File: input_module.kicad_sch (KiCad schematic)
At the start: 13 parts, among them Q14 BC846

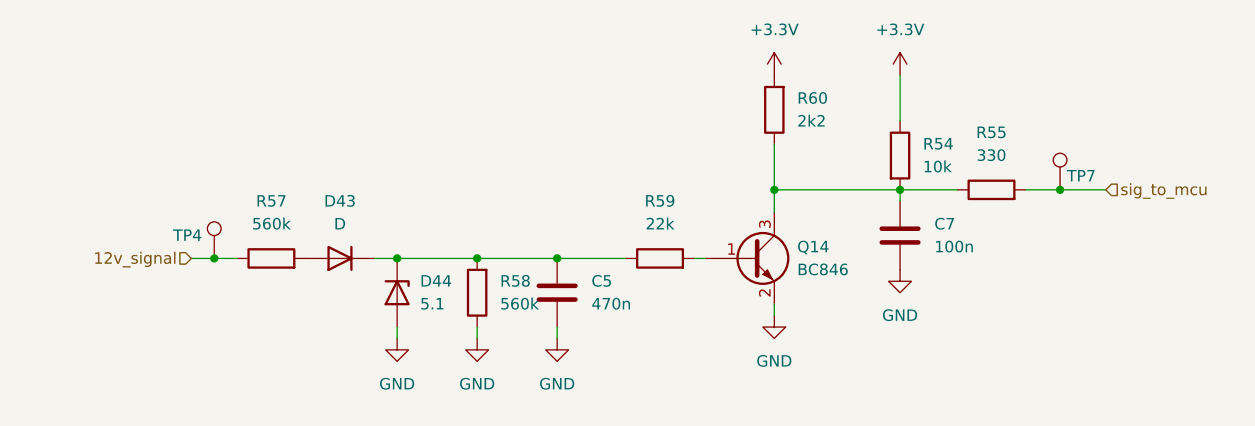
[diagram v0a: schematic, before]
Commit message: Schematic sites change
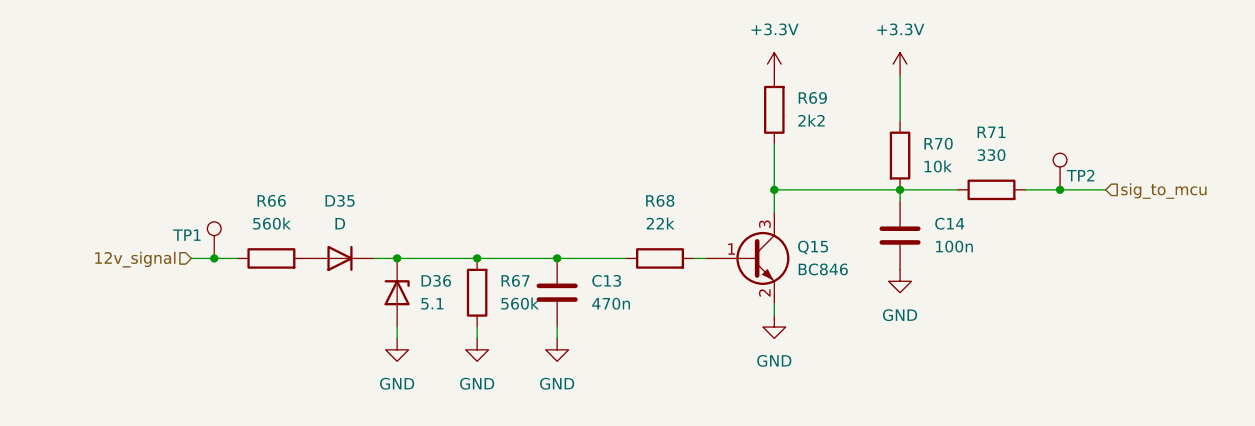
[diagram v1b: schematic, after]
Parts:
- renumbered C5 to C13, C7 to C14, D43 to D35, D44 to D36, Q14 to Q15, R57 to R66, R58 to R67, R59 to R68, R60 to R69, R54 to R70, R55 to R71, TP4 to TP1, TP7 to TP2

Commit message: mos leds drivers
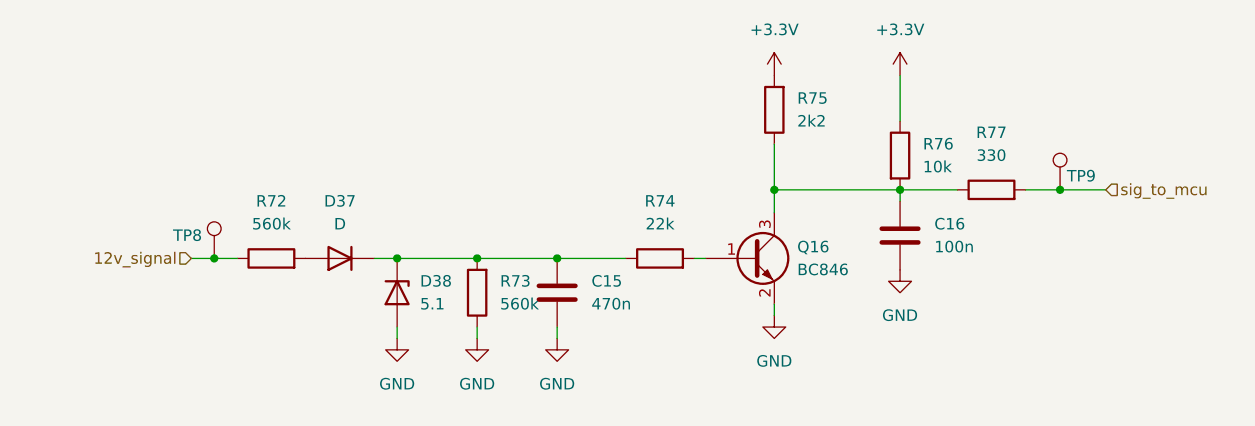
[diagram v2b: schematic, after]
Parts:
- renumbered C13 to C15, C14 to C16, D35 to D37, D36 to D38, Q15 to Q16, R66 to R72, R67 to R73, R68 to R74, R69 to R75, R70 to R76, R71 to R77, TP1 to TP8, TP2 to TP9
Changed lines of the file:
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@@
 		(dnp no)
 		(fields_autoplaced yes)
-		(property "Reference" "C13"
+		(property "Reference" "C15"
 			(at 118.11 62.2299 0)
 			(effects
@@
 		(on_board yes)
 		(dnp no)
-		(property "Reference" "TP1"
+		(property "Reference" "TP8"
 			(at 71.628 57.15 0)
 			(effects
@@
 		(dnp no)
 		(fields_autoplaced yes)
-		(property "Reference" "R67"
+		(property "Reference" "R73"
 			(at 107.95 62.2299 0)
 			(effects
@@
 		(dnp no)
 		(fields_autoplaced yes)
-		(property "Reference" "R68"
+		(property "Reference" "R74"
 			(at 125.73 53.34 90)
 			(effects
@@
 		(dnp no)
 		(fields_autoplaced yes)
-		(property "Reference" "#PWR061"
+		(property "Reference" "#PWR068"
 			(at 152.4 67.31 0)
 			(effects
@@
 		(on_board yes)
 		(dnp no)
-		(property "Reference" "TP2"
+		(property "Reference" "TP9"
 			(at 170.942 50.546 0)
 			(effects
@@
 		(dnp no)
 		(fields_autoplaced yes)
-		(property "Reference" "#PWR056"
+		(property "Reference" "#PWR063"
 			(at 105.41 74.93 0)
 			(effects
@@
 		(dnp no)
 		(fields_autoplaced yes)
-		(property "Reference" "R70"
+		(property "Reference" "R76"
 			(at 154.94 46.9899 0)
 			(effects
@@
 		(dnp no)
 		(fields_autoplaced yes)
-		(property "Reference" "R69"
+		(property "Reference" "R75"
 			(at 140.97 41.9099 0)
 			(effects
@@
 		(dnp no)
 		(fields_autoplaced yes)
-		(property "Reference" "D35"
+		(property "Reference" "D37"
 			(at 90.17 53.34 0)
 			(effects
@@
 		(dnp no)
 		(fields_autoplaced yes)
-		(property "Reference" "#PWR055"
+		(property "Reference" "#PWR062"
 			(at 96.52 74.93 0)
 			(effects
@@
 		(dnp no)
 		(fields_autoplaced yes)
-		(property "Reference" "R71"
+		(property "Reference" "R77"
 			(at 162.56 45.72 90)
 			(effects
@@
 		(dnp no)
 		(fields_autoplaced yes)
-		(property "Reference" "#PWR058"
+		(property "Reference" "#PWR065"
 			(at 138.43 43.18 0)
 			(effects
@@
 		(dnp no)
 		(fields_autoplaced yes)
-		(property "Reference" "#PWR059"
+		(property "Reference" "#PWR066"
 			(at 138.43 72.39 0)
 			(effects
@@
 		(dnp no)
 		(fields_autoplaced yes)
-		(property "Reference" "C14"
+		(property "Reference" "C16"
 			(at 156.21 55.8799 0)
 			(effects
@@
 		(dnp no)
 		(fields_autoplaced yes)
-		(property "Reference" "#PWR060"
+		(property "Reference" "#PWR067"
 			(at 152.4 43.18 0)
 			(effects
@@
 		(dnp no)
 		(fields_autoplaced yes)
-		(property "Reference" "R66"
+		(property "Reference" "R72"
 			(at 82.55 53.34 90)
 			(effects
@@
 		(dnp no)
 		(fields_autoplaced yes)
-		(property "Reference" "Q15"
+		(property "Reference" "Q16"
 			(at 140.97 58.4199 0)
 			(effects
@@
 		(dnp no)
 		(fields_autoplaced yes)
-		(property "Reference" "#PWR057"
+		(property "Reference" "#PWR064"
 			(at 114.3 74.93 0)
 			(effects
@@
 		(dnp no)
 		(fields_autoplaced yes)
-		(property "Reference" "D36"
+		(property "Reference" "D38"
 			(at 99.06 62.2299 90)
 			(effects

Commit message: New template
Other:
- company: (none) -> STAPsystem
- title: (none) -> RPM meter LED
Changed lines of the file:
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@@
 	(generator_version "8.0")
 	(paper "A4")
+	(title_block
+		(title "RPM meter LED")
+		(date "2024-11-26")
+		(rev "v1.0")
+		(company "STAPsystem")
+	)
 	(junction
 		(at 76.2 59.69)

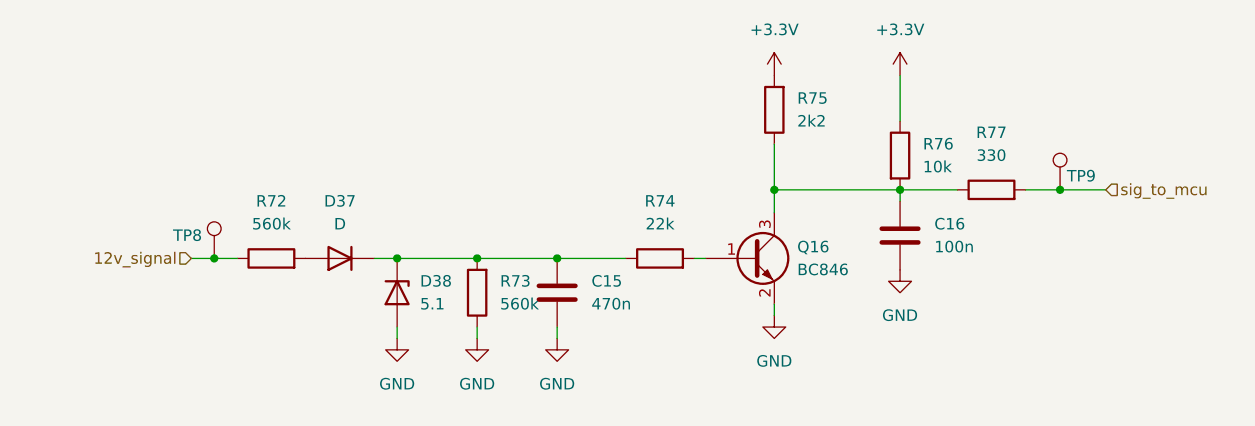
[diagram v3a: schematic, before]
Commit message: TVS protection
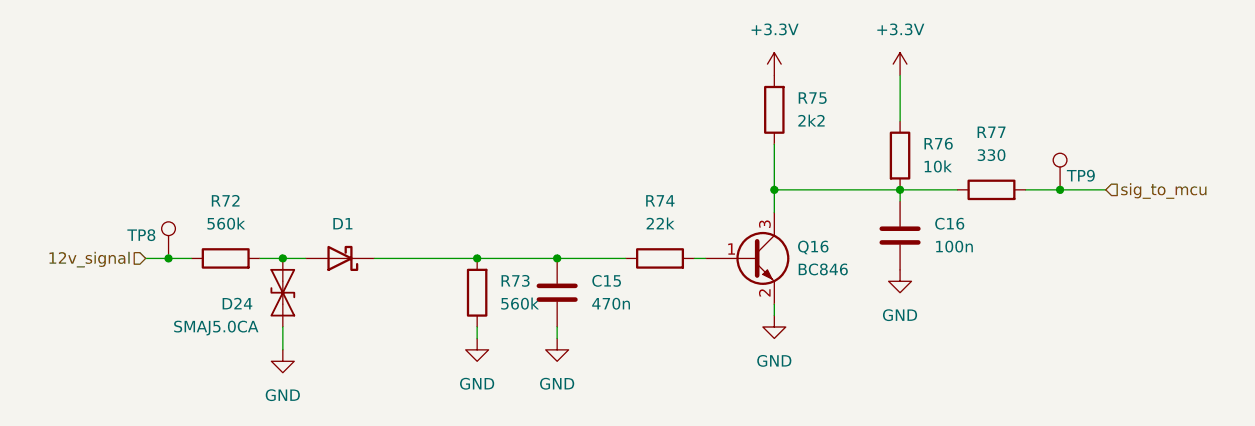
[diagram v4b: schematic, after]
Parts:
- removed D37: D, Diode_SMD:D_0805_2012Metric, symbol Device:D
- removed D38: 5.1, Diode_SMD:D_0805_2012Metric, symbol Device:D_Zener
- added D1: D_Schottky, Diode_SMD:D_0603_1608Metric, symbol Device:D_Schottky
- added D24: SMAJ5.0CA, Diode_SMD:D_SMA, symbol Diode:SMAJ5.0CA
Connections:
- net GND: now also D24.1 (A1)
- net at C15.1, R73.2, R74.1: now also D1.1 (K)
- net at R72.2: now also D1.2 (A), D24.2 (A2)
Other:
- moved on the sheet: R72, TP8

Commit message: todo
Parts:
- renumbered D24 to D26, D1 to D29
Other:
- note added: "niepotrzebne"
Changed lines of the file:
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@@
+		)
+	)
+	(text "niepotrzebne"
+		(exclude_from_sim no)
+		(at 152.654 43.434 0)
+		(effects
+			(font
+				(size 1.27 1.27)
+			)
 		)
 	)
@@
 		(on_board yes)
 		(dnp no)
-		(property "Reference" "D24"
+		(property "Reference" "D26"
 			(at 76.962 64.77 90)
 			(effects
@@
 		(dnp no)
 		(fields_autoplaced yes)
-		(property "Reference" "#PWR092"
+		(property "Reference" "#PWR094"
 			(at 83.82 76.2 0)
 			(effects
@@
 		(dnp no)
 		(fields_autoplaced yes)
-		(property "Reference" "D1"
+		(property "Reference" "D29"
 			(at 90.4875 55.88 0)
 			(effects

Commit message: Placed footprints v1.0
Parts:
- removed D29: D_Schottky, Diode_SMD:D_0603_1608Metric, symbol Device:D_Schottky
- removed TP8, TP9: TestPoint, TestPoint:TestPoint_Loop_D1.80mm_Drill1.0mm_Beaded, symbol Connector:TestPoint
- R72: footprint Resistor_SMD:R_0603_1608Metric -> Resistor_SMD:R_2512_6332Metric
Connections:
- net at C15.1, R73.2, R74.1: now also D26.2 (A2), R72.2

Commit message: 2.1
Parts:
- R76: now not fitted; now left out of the parts list
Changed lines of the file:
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@@
 		(unit 1)
 		(exclude_from_sim no)
-		(in_bom yes)
+		(in_bom no)
 		(on_board yes)
-		(dnp no)
+		(dnp yes)
 		(fields_autoplaced yes)
 		(property "Reference" "R76"
